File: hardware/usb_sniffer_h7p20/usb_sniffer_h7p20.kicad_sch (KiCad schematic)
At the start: 97 parts, among them J1 FPGA_JTAG, J4 USB_C_Receptacle_USB2.0_16P, J5 FFC-40P-0.5mm,NC, U1 H7P20N0L128-M3H1, U6 P25Q32SH-SSH-IT, U7 CY7C68013A-56LTX, U8 24C64BN, U9 CJ3439KDW, X1 XO32,26M,NC, Y2 24M

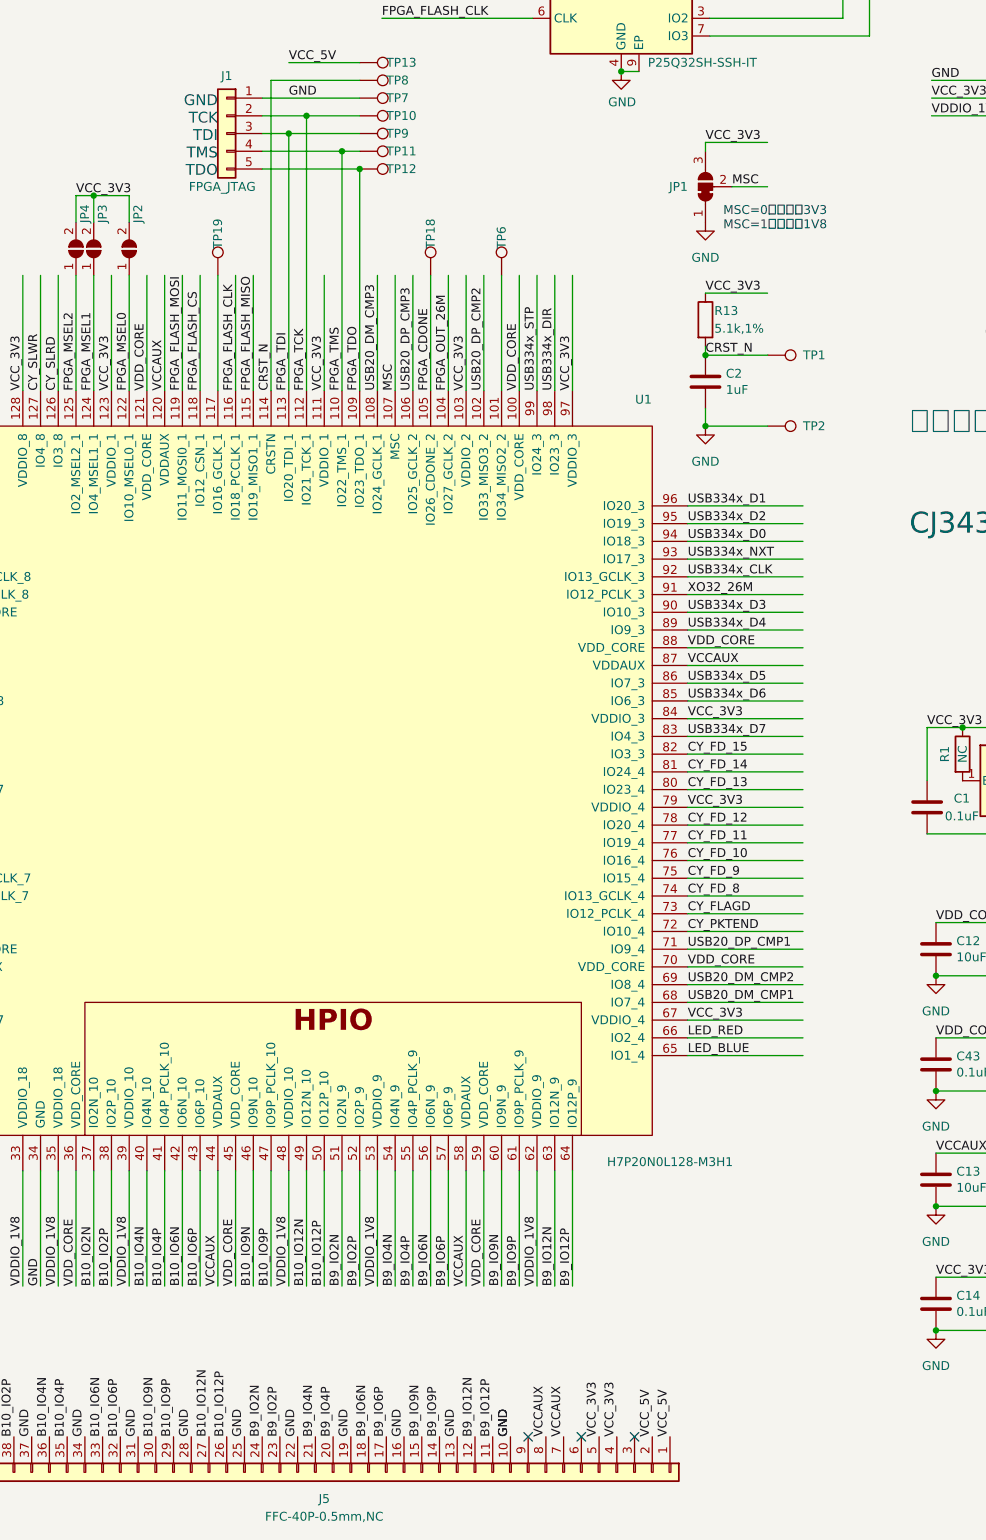
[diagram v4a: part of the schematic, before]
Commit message: [usb_sniffer_h7p20] 结构优化与验证
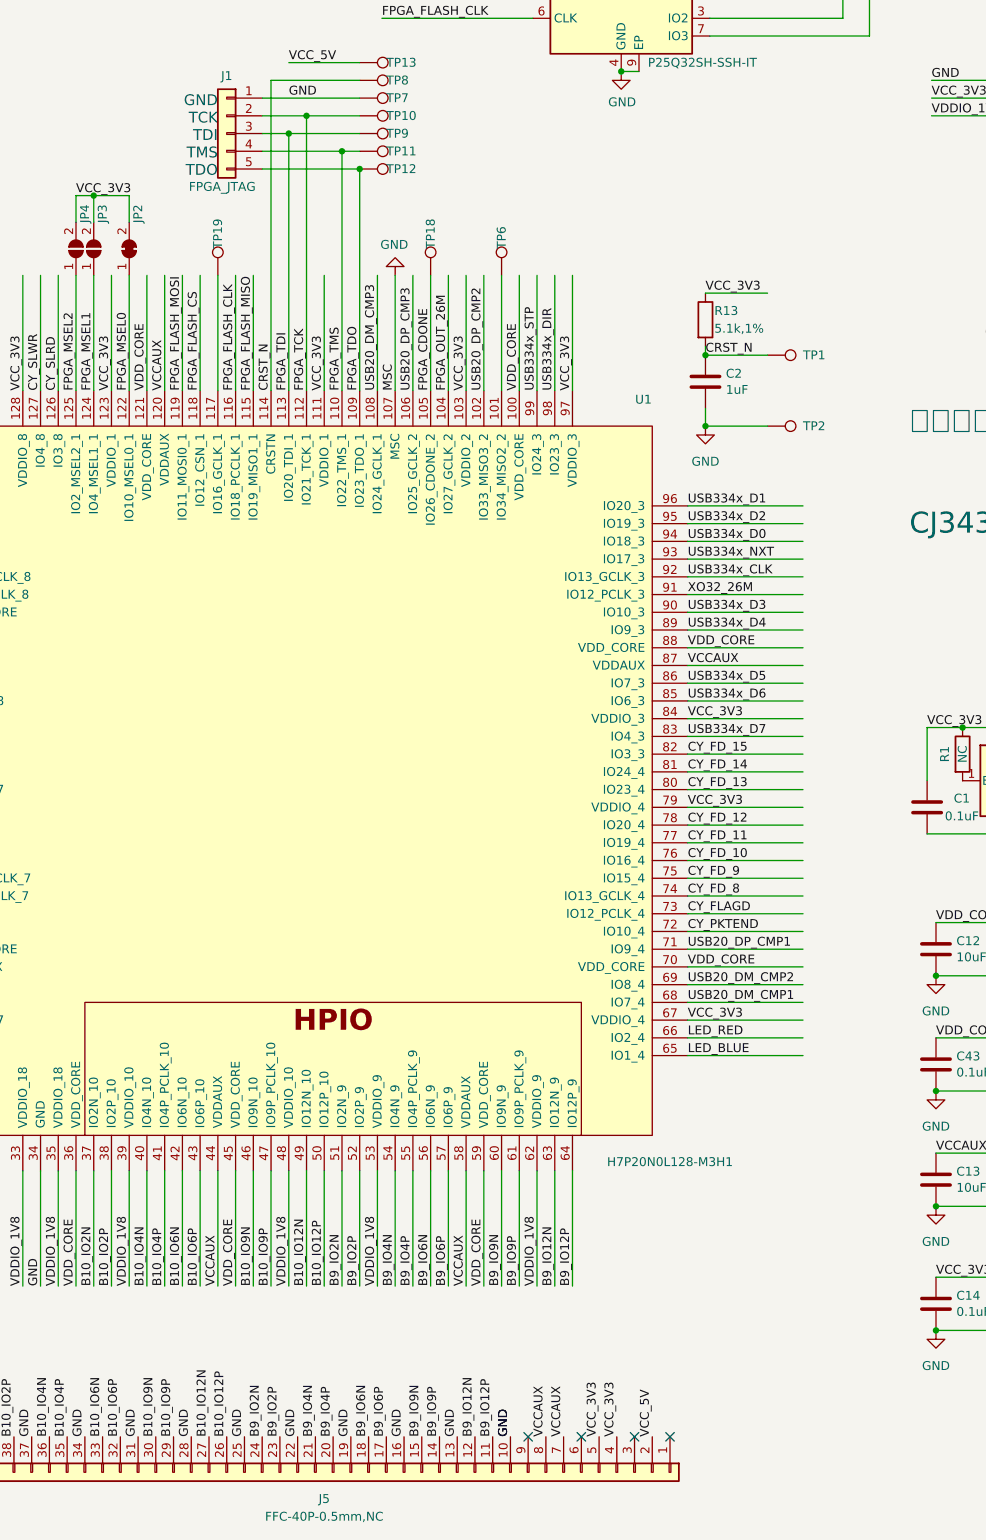
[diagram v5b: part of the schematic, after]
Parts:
- removed JP1: SolderJumper_3_Bridged12, Jumper:SolderJumper-3_P1.3mm_Bridged12_RoundedPad1.0x1.5mm_NumberLabels, symbol Jumper:SolderJumper_3_Bridged12
- removed JP2: SolderJumper_2_Open, Jumper:SolderJumper-2_P1.3mm_Open_RoundedPad1.0x1.5mm, symbol Jumper:SolderJumper_2_Open
- added JP2: SolderJumper_2_Bridged, Jumper:SolderJumper-2_P1.3mm_Bridged_RoundedPad1.0x1.5mm, symbol Jumper:SolderJumper_2_Bridged
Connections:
- net MSC is gone; now on net GND: U1.107 (MSC)
- net FPGA_MSEL0: now also JP2.1 (A)
- net VCC_3V3: now also JP2.2 (B)
- net VCC_5V: no longer J5.1 (Pin_1)
- no-connect marks 5 -> 6
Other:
- note removed: "MSC=0：配置脚3V3 MSC=1：配置脚1V8"
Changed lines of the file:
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@@
   (no_connect (at 134.62 115.57))
   (no_connect (at 134.62 118.11))
+  (no_connect (at 243.84 246.38))
   (no_connect (at 238.76 246.38))
   (no_connect (at 231.14 246.38))
@@
     (stroke (width 0) (type default))
   )
-  (wire (pts (xy 248.92 60.96) (xy 257.81 60.96))
-    (stroke (width 0) (type default))
-  )
   (wire (pts (xy 212.09 224.79) (xy 212.09 208.28))
     (stroke (width 0) (type default))
@@
     (stroke (width 0) (type default))
   )
-  (wire (pts (xy 252.73 67.31) (xy 257.81 67.31))
-    (stroke (width 0) (type default))
-  )
   (wire (pts (xy 367.03 54.61) (xy 350.52 54.61))
     (stroke (width 0) (type default))
@@
     (stroke (width 0) (type default))
   )
-  (wire (pts (xy 248.92 62.23) (xy 248.92 60.96))
-    (stroke (width 0) (type default))
-  )
   (wire (pts (xy 350.52 29.21) (xy 367.03 29.21))
     (stroke (width 0) (type default))
@@
     (effects (font (size 1.55 1.55)) (justify right bottom))
   )
-  (text "MSC=0：配置脚3V3\nMSC=1：配置脚1V8" (at 251.46 73.66 0)
-    (effects (font (size 1.27 1.27)) (justify left bottom))
-  )
   (text "上电顺序：VCC_5V --- 0R          >>> OUT1(0.95V)\n                 --- 10k 1uF RC  >>> OUT2(VCCAUX)\n                 --- 20k 1uF RC  >>> OUT3(3.3V)\nCJ3439KDW在3.3V上电后，导通VCCAUX到VDDIO_1V8"
     (at 278.13 117.475 0)
@@
     (effects (font (size 1.27 1.27)) (justify left bottom))
   )
-  (label "VCC_5V" (at 243.84 246.38 90) (fields_autoplaced)
-    (effects (font (size 1.27 1.27)) (justify left bottom))
-  )
   (label "USB334x_CLK" (at 350.52 34.29 0) (fields_autoplaced)
     (effects (font (size 1.27 1.27)) (justify left bottom))
@@
     (effects (font (size 1.27 1.27)) (justify left bottom))
   )
-  (label "MSC" (at 252.73 67.31 0) (fields_autoplaced)
-    (effects (font (size 1.27 1.27)) (justify left bottom))
-  )
   (label "USB334x_D6" (at 350.52 52.07 0) (fields_autoplaced)
     (effects (font (size 1.27 1.27)) (justify left bottom))
@@
     (effects (font (size 1.27 1.27)) (justify left bottom))
   )
-  (label "VCC_3V3" (at 248.92 60.96 0) (fields_autoplaced)
-    (effects (font (size 1.27 1.27)) (justify left bottom))
-  )
   (label "VDDIO_1V8" (at 281.305 57.15 0) (fields_autoplaced)
     (effects (font (size 1.27 1.27)) (justify left bottom))
@@
     )
   )
-  (symbol (lib_id "Jumper:SolderJumper_2_Open") (at 166.37 76.2 90) (unit 1)
-    (in_bom yes) (on_board yes) (dnp no)
-    (property "Reference" "JP2" (at 167.64 69.85 0)
-      (effects (font (size 1.27 1.27)) (justify right))
-    )
-    (property "Value" "SolderJumper_2_Open" (at 168.91 77.47 90)
-      (effects (font (size 1.27 1.27)) (justify right) hide)
-    )
-    (property "Footprint" "Jumper:SolderJumper-2_P1.3mm_Open_RoundedPad1.0x1.5mm" (at 166.37 76.2 0)
-      (effects (font (size 1.27 1.27)) hide)
-    )
-    (property "Datasheet" "~" (at 166.37 76.2 0)
-      (effects (font (size 1.27 1.27)) hide)
-    )
-    (pin "1")
-    (pin "2")
-    (instances
-      (project "usb_sniffer_h7p20"
-        (path "/5a8287a8-9f7a-4e60-a3bf-19c1227b20fe"
-          (reference "JP2") (unit 1)
-        )
-      )
-    )
-  )
   (symbol (lib_id "Device:LED") (at 121.92 43.18 180) (unit 1)
     (in_bom yes) (on_board yes) (dnp no)
@@
     )
   )
-  (symbol (lib_id "power:GND") (at 134.62 43.18 0) (unit 1)
-    (in_bom yes) (on_board yes) (dnp no) (fields_autoplaced)
-    (property "Reference" "#PWR052" (at 134.62 49.53 0)
+  (symbol (lib_id "power:GND") (at 204.47 80.01 180) (unit 1)
+    (in_bom yes) (on_board yes) (dnp no)
+    (property "Reference" "#PWR02" (at 204.47 73.66 0)
       (effects (font (size 1.27 1.27)) hide)
     )
-    (property "Value" "GND" (at 134.62 48.26 0)
+    (property "Value" "GND" (at 204.343 75.6158 0)
       (effects (font (size 1.27 1.27)))
     )
-    (property "Footprint" "" (at 134.62 43.18 0)
+    (property "Footprint" "" (at 204.47 80.01 0)
       (effects (font (size 1.27 1.27)) hide)
     )
-    (property "Datasheet" "" (at 134.62 43.18 0)
+    (property "Datasheet" "" (at 204.47 80.01 0)
       (effects (font (size 1.27 1.27)) hide)
     )
@@
       (project "usb_sniffer_h7p20"
         (path "/5a8287a8-9f7a-4e60-a3bf-19c1227b20fe"
-          (reference "#PWR052") (unit 1)
+          (reference "#PWR02") (unit 1)
         )
       )
     )
   )
-  (symbol (lib_id "Jumper:SolderJumper_3_Bridged12") (at 248.92 67.31 90) (unit 1)
+  (symbol (lib_id "power:GND") (at 134.62 43.18 0) (unit 1)
     (in_bom yes) (on_board yes) (dnp no) (fields_autoplaced)
-    (property "Reference" "JP1" (at 246.38 67.31 90)
-      (effects (font (size 1.27 1.27)) (justify left))
-    )
-    (property "Value" "SolderJumper_3_Bridged12" (at 245.11 67.31 0)
+    (property "Reference" "#PWR052" (at 134.62 49.53 0)
       (effects (font (size 1.27 1.27)) hide)
     )
-    (property "Footprint" "Jumper:SolderJumper-3_P1.3mm_Bridged12_RoundedPad1.0x1.5mm_NumberLabels" (at 248.92 67.31 0)
+    (property "Value" "GND" (at 134.62 48.26 0)
+      (effects (font (size 1.27 1.27)))
+    )
+    (property "Footprint" "" (at 134.62 43.18 0)
       (effects (font (size 1.27 1.27)) hide)
     )
-    (property "Datasheet" "~" (at 248.92 67.31 0)
+    (property "Datasheet" "" (at 134.62 43.18 0)
       (effects (font (size 1.27 1.27)) hide)
     )
-    (pin "2")
     (pin "1")
-    (pin "3")
     (instances
       (project "usb_sniffer_h7p20"
         (path "/5a8287a8-9f7a-4e60-a3bf-19c1227b20fe"
-          (reference "JP1") (unit 1)
+          (reference "#PWR052") (unit 1)
         )
       )
@@
     )
   )
-  (symbol (lib_id "power:GND") (at 248.92 72.39 0) (unit 1)
-    (in_bom yes) (on_board yes) (dnp no) (fields_autoplaced)
-    (property "Reference" "#PWR03" (at 248.92 78.74 0)
-      (effects (font (size 1.27 1.27)) hide)
-    )
-    (property "Value" "GND" (at 248.92 77.47 0)
-      (effects (font (size 1.27 1.27)))
-    )
-    (property "Footprint" "" (at 248.92 72.39 0)
-      (effects (font (size 1.27 1.27)) hide)
-    )
-    (property "Datasheet" "" (at 248.92 72.39 0)
-      (effects (font (size 1.27 1.27)) hide)
-    )
-    (pin "1")
-    (instances
-      (project "usb_sniffer_h7p20"
-        (path "/5a8287a8-9f7a-4e60-a3bf-19c1227b20fe"
-          (reference "#PWR03") (unit 1)
-        )
-      )
-    )
-  )
   (symbol (lib_id "Connector:TestPoint") (at 219.71 80.01 0) (unit 1)
     (in_bom yes) (on_board yes) (dnp no)
@@
         )
       )
+    )
+  )
+  (symbol (lib_id "Jumper:SolderJumper_2_Bridged") (at 166.37 76.2 90) (unit 1)
+    (in_bom yes) (on_board yes) (dnp no)
+    (property "Reference" "JP2" (at 167.64 69.85 0)
+      (effects (font (size 1.27 1.27)) (justify right))
+    )
+    (property "Value" "SolderJumper_2_Bridged" (at 168.91 77.47 90)
+      (effects (font (size 1.27 1.27)) (justify right) hide)
+    )
+    (property "Footprint" "Jumper:SolderJumper-2_P1.3mm_Bridged_RoundedPad1.0x1.5mm" (at 166.37 76.2 0)
+      (effects (font (size 1.27 1.27)) hide)
+    )
+    (property "Datasheet" "~" (at 166.37 76.2 0)
+      (effects (font (size 1.27 1.27)) hide)
+    )
+    (pin "2")
+    (pin "1")
+    (instances
+      (project "usb_sniffer_h7p20"
+        (path "/5a8287a8-9f7a-4e60-a3bf-19c1227b20fe"
+          (reference "JP2") (unit 1)
+        )
+      )

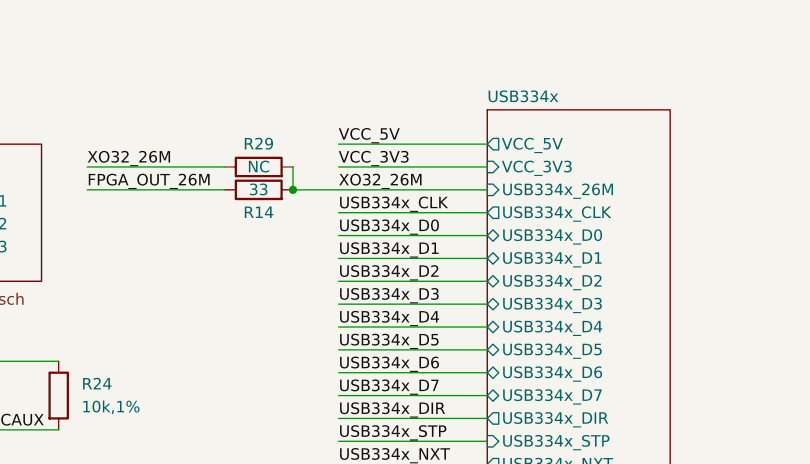
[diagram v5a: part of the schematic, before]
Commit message: [usb_sniffer_h7p20] 修复USB3343参考时钟电路错误；修复USB3343 RESET脚上拉错误
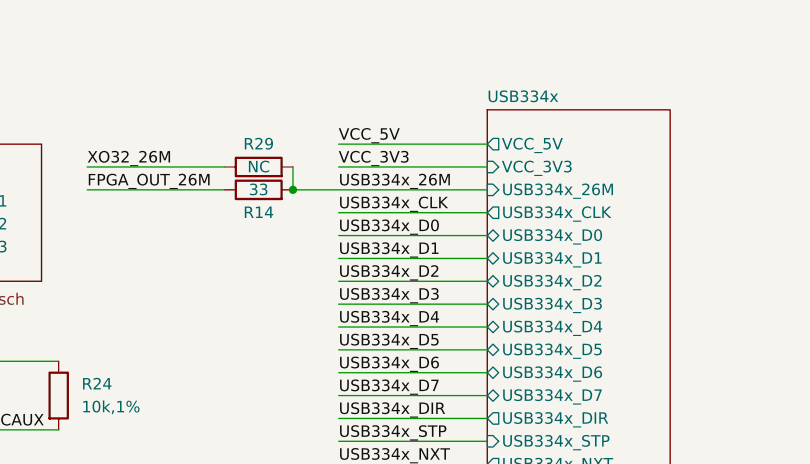
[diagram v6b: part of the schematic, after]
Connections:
- net XO32_26M: no longer R14.2, R29.2
- new net USB334x_26M: R14.2, R29.2
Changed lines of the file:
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@@
+    (effects (font (size 1.27 1.27)) (justify left bottom))
+  )
+  (label "USB334x_26M" (at 350.52 31.75 0) (fields_autoplaced)
     (effects (font (size 1.27 1.27)) (justify left bottom))
   )
@@
     (effects (font (size 1.27 1.27)) (justify left bottom))
   )
-  (label "XO32_26M" (at 350.52 31.75 0) (fields_autoplaced)
-    (effects (font (size 1.27 1.27)) (justify left bottom))
-  )

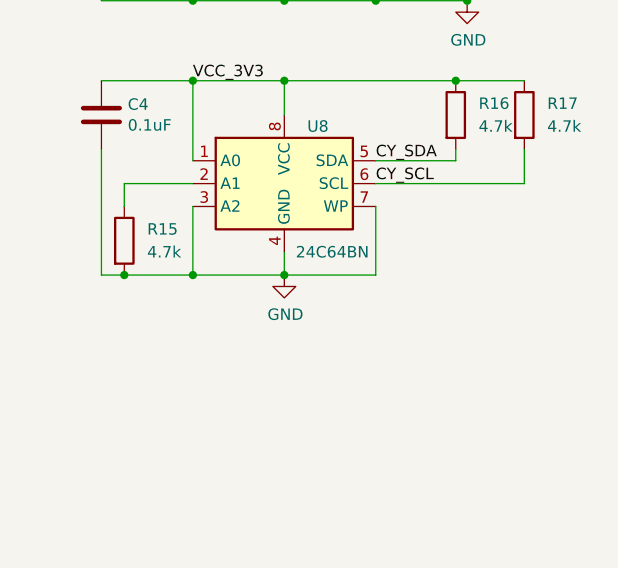
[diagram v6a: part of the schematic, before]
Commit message: [usb_sniffer_h7p20] 68013的eeprom增加boot点，用于二次更新68013固件
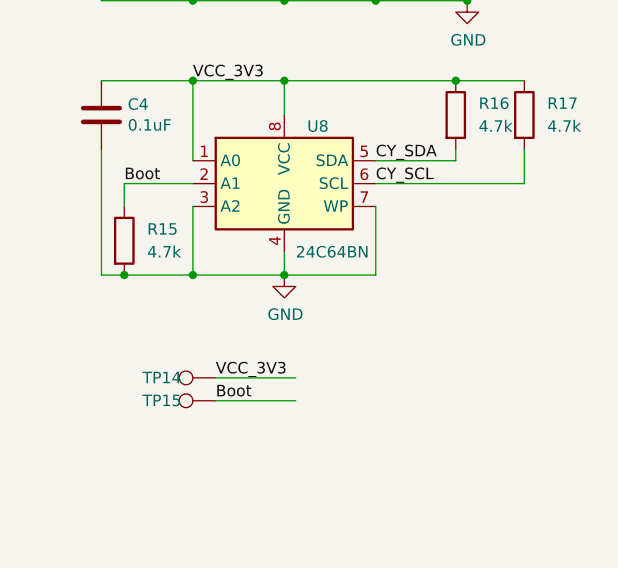
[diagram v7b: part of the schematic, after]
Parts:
- added TP14, TP15: TestPoint, vllogic:PinHeader_1x01_P1.00mm_Vertical, symbol Connector:TestPoint
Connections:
- net VCC_3V3: now also TP14.1
- net Boot: now reaches R15.1, U8.2 (A1)
- net Boot: now also TP15.1
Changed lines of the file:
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@@
     (stroke (width 0) (type default))
   )
+  (wire (pts (xy 35.56 242.57) (xy 44.45 242.57))
+    (stroke (width 0) (type default))
+  )
   (wire (pts (xy 262.89 120.65) (xy 246.38 120.65))
     (stroke (width 0) (type default))
@@
     (stroke (width 0) (type default))
   )
+  (wire (pts (xy 35.56 240.03) (xy 44.45 240.03))
+    (stroke (width 0) (type default))
+  )
   (wire (pts (xy 20.32 110.49) (xy 46.99 110.49))
     (stroke (width 0) (type default))
@@
     (effects (font (size 1.27 1.27)) (justify left bottom))
   )
+  (label "Boot" (at 35.56 242.57 0) (fields_autoplaced)
+    (effects (font (size 1.27 1.27)) (justify left bottom))
+  )
   (label "CY_FD_8" (at 246.38 168.91 0) (fields_autoplaced)
     (effects (font (size 1.27 1.27)) (justify left bottom))
@@
     (effects (font (size 1.27 1.27)) (justify left bottom))
   )
+  (label "Boot" (at 25.4 218.44 0) (fields_autoplaced)
+    (effects (font (size 1.27 1.27)) (justify left bottom))
+  )
   (label "GND" (at 189.23 54.61 0) (fields_autoplaced)
     (effects (font (size 1.27 1.27)) (justify left bottom))
@@
     (effects (font (size 1.27 1.27)) (justify left bottom))
   )
+  (label "VCC_3V3" (at 35.56 240.03 0) (fields_autoplaced)
+    (effects (font (size 1.27 1.27)) (justify left bottom))
+  )
   (label "CY_FD_2" (at 82.55 92.71 0) (fields_autoplaced)
     (effects (font (size 1.27 1.27)) (justify left bottom))
@@
     )
   )
+  (symbol (lib_id "Connector:TestPoint") (at 35.56 240.03 90) (unit 1)
+    (in_bom yes) (on_board yes) (dnp no)
+    (property "Reference" "TP14" (at 31.75 240.03 90)
+      (effects (font (size 1.27 1.27)) (justify left))
+    )
+    (property "Value" "TestPoint" (at 30.48 238.76 90)
+      (effects (font (size 1.27 1.27)) (justify left) hide)
+    )
+    (property "Footprint" "vllogic:PinHeader_1x01_P1.00mm_Vertical" (at 35.56 234.95 0)
+      (effects (font (size 1.27 1.27)) hide)
+    )
+    (property "Datasheet" "~" (at 35.56 234.95 0)
+      (effects (font (size 1.27 1.27)) hide)
+    )
+    (pin "1")
+    (instances
+      (project "usb_sniffer_h7p20"
+        (path "/5a8287a8-9f7a-4e60-a3bf-19c1227b20fe"
+          (reference "TP14") (unit 1)
+        )
+      )
+    )
+  )
   (symbol (lib_id "Device:C") (at 281.94 209.55 180) (unit 1)
     (in_bom yes) (on_board yes) (dnp no)
@@
         )
       )
+    )
+  )
+  (symbol (lib_id "Connector:TestPoint") (at 35.56 242.57 90) (unit 1)
+    (in_bom yes) (on_board yes) (dnp no)
+    (property "Reference" "TP15" (at 31.75 242.57 90)
+      (effects (font (size 1.27 1.27)) (justify left))
+    )
+    (property "Value" "TestPoint" (at 30.48 241.3 90)
+      (effects (font (size 1.27 1.27)) (justify left) hide)
+    )
+    (property "Footprint" "vllogic:PinHeader_1x01_P1.00mm_Vertical" (at 35.56 237.49 0)
+      (effects (font (size 1.27 1.27)) hide)
+    )
+    (property "Datasheet" "~" (at 35.56 237.49 0)
+      (effects (font (size 1.27 1.27)) hide)
+    )
+    (pin "1")
+    (instances
+      (project "usb_sniffer_h7p20"
+        (path "/5a8287a8-9f7a-4e60-a3bf-19c1227b20fe"
+          (reference "TP15") (unit 1)
+        )
+      )
